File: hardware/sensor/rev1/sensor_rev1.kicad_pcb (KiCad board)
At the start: 2 copper layers, 28.9 x 68.9 mm, 52 parts, among them IC1 STM8L051F3P6, IC2 CC1101RGPR, J1 22-28-4044, J2 M20-9770342, Y1 NX3225GA-26.000M-STD-CRG-2

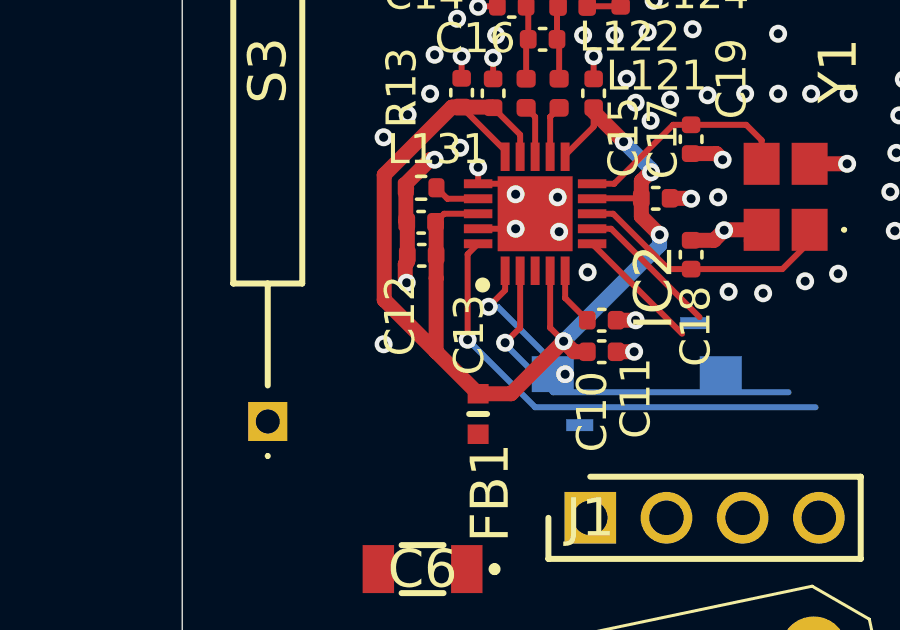
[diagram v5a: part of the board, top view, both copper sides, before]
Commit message: EG-49 Removed a bulk capacitor.
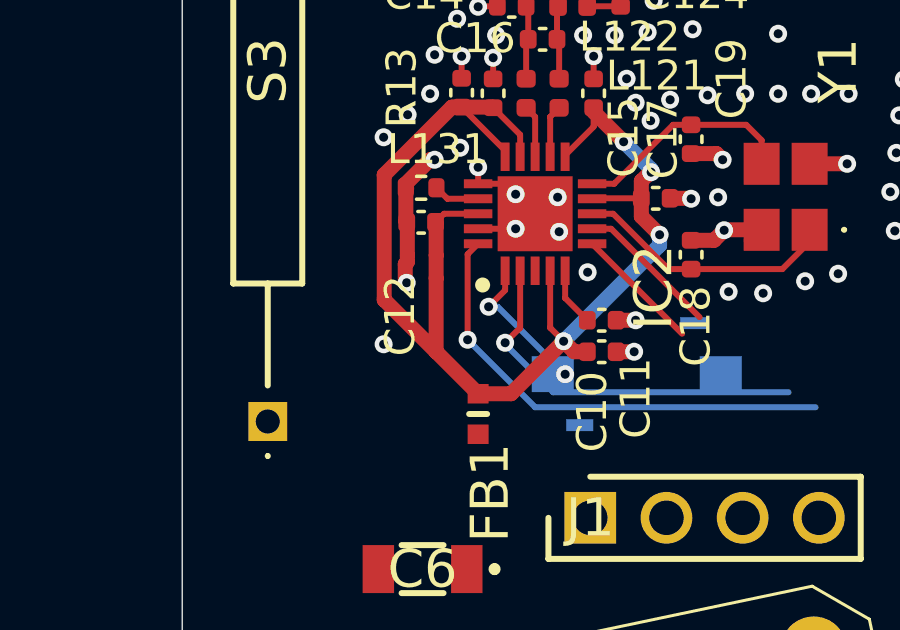
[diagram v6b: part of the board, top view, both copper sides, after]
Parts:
- removed C13: 1uF, Capacitor_SMD:C_0402_1005Metric
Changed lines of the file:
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@@
 	(net 34 "unconnected-(S2-GND_1-Pad3)")
 	(net 35 "unconnected-(S2-GND_2-Pad4)")
-	(footprint "Capacitor_SMD:C_0402_1005Metric"
-		(layer "F.Cu")
-		(at 227.9821 115.43 180)
-		(descr "Capacitor SMD 0402 (1005 Metric), square (rectangular) end terminal, IPC_7351 nominal, (Body size source: IPC-SM-782 page 76, https://www.pcb-3d.com/wordpress/wp-content/uploads/ipc-sm-782a_amendment_1_and_2.pdf), generated with kicad-footprint-generator")
-		(tags "capacitor")
-		(property "Reference" "C13"
-			(at -1.58 -2.65 90)
-			(layer "F.SilkS")
-			(effects
-				(font
-					(size 1 1)
-					(thickness 0.15)
-				)
-			)
-		)
-		(property "Value" "1uF"
-			(at 0 1.16 0)
-			(layer "F.Fab")
-			(effects
-				(font
-					(size 1 1)
-					(thickness 0.15)
-				)
-			)
-		)
-		(property "Datasheet" "~"
-			(at 0 0 180)
-			(unlocked yes)
-			(layer "F.Fab")
-			(hide yes)
-			(effects
-				(font
-					(size 1.27 1.27)
-					(thickness 0.15)
-				)
-			)
-		)
-		(property "Description" "Unpolarized capacitor"
-			(at 0 0 180)
-			(unlocked yes)
-			(layer "F.Fab")
-			(hide yes)
-			(effects
-				(font
-					(size 1.27 1.27)
-					(thickness 0.15)
-				)
-			)
-		)
-		(property "Mouser Part Number" "81-GXT155R60J105KE1D"
-			(at 0 0 180)
-			(unlocked yes)
-			(layer "F.Fab")
-			(hide yes)
-			(effects
-				(font
-					(size 1 1)
-					(thickness 0.15)
-				)
-			)
-		)
-		(property "Supplier Link" "https://pt.mouser.com/ProductDetail/Murata-Electronics/GXT155R60J105KE01D?qs=d0WKAl%252BL4Kb4JfV7cPss8A%3D%3D"
-			(at 0 0 180)
-			(unlocked yes)
-			(layer "F.Fab")
-			(hide yes)
-			(effects
-				(font
-					(size 1 1)
-					(thickness 0.15)
-				)
-			)
-		)
-		(property "Manufacturer" "Murata"
-			(at 0 0 180)
-			(unlocked yes)
-			(layer "F.Fab")
-			(hide yes)
-			(effects
-				(font
-					(size 1 1)
-					(thickness 0.15)
-				)
-			)
-		)
-		(property "Manufacturer Part Number" "GXT155R60J105KE01D "
-			(at 0 0 180)
-			(unlocked yes)
-			(layer "F.Fab")
-			(hide yes)
-			(effects
-				(font
-					(size 1 1)
-					(thickness 0.15)
-				)
-			)
-		)
-		(property ki_fp_filters "C_*")
-		(sheetname "/RF/")
-		(sheetfile "rf_rev1.kicad_sch")
-		(attr smd)
-		(fp_line
-			(start -0.107836 0.36)
-			(end 0.107836 0.36)
-			(stroke
-				(width 0.12)
-				(type solid)
-			)
-			(layer "F.SilkS")
-		)
-		(fp_line
-			(start -0.107836 -0.36)
-			(end 0.107836 -0.36)
-			(stroke
-				(width 0.12)
-				(type solid)
-			)
-			(layer "F.SilkS")
-		)
-		(fp_line
-			(start 0.91 0.46)
-			(end -0.91 0.46)
-			(stroke
-				(width 0.05)
-				(type solid)
-			)
-			(layer "F.CrtYd")
-		)
-		(fp_line
-			(start 0.91 -0.46)
-			(end 0.91 0.46)
-			(stroke
-				(width 0.05)
-				(type solid)
-			)
-			(layer "F.CrtYd")
-		)
-		(fp_line
-			(start -0.91 0.46)
-			(end -0.91 -0.46)
-			(stroke
-				(width 0.05)
-				(type solid)
-			)
-			(layer "F.CrtYd")
-		)
-		(fp_line
-			(start -0.91 -0.46)
-			(end 0.91 -0.46)
-			(stroke
-				(width 0.05)
-				(type solid)
-			)
-			(layer "F.CrtYd")
-		)
-		(fp_line
-			(start 0.5 0.25)
-			(end -0.5 0.25)
-			(stroke
-				(width 0.1)
-				(type solid)
-			)
-			(layer "F.Fab")
-		)
-		(fp_line
-			(start 0.5 -0.25)
-			(end 0.5 0.25)
-			(stroke
-				(width 0.1)
-				(type solid)
-			)
-			(layer "F.Fab")
-		)
-		(fp_line
-			(start -0.5 0.25)
-			(end -0.5 -0.25)
-			(stroke
-				(width 0.1)
-				(type solid)
-			)
-			(layer "F.Fab")
-		)
-		(fp_line
-			(start -0.5 -0.25)
-			(end 0.5 -0.25)
-			(stroke
-				(width 0.1)
-				(type solid)
-			)
-			(layer "F.Fab")
-		)
-		(fp_text user "${REFERENCE}"
-			(at 0 0 0)
-			(layer "F.Fab")
-			(effects
-				(font
-					(size 0.25 0.25)
-					(thickness 0.04)
-				)
-			)
-		)
-		(pad "1" smd roundrect
-			(at -0.48 0 180)
-			(size 0.56 0.62)
-			(layers "F.Cu" "F.Mask" "F.Paste")
-			(roundrect_rratio 0.25)
-			(net 7 "RF_VDD")
-			(pintype "passive")
-		)
-		(pad "2" smd roundrect
-			(at 0.48 0 180)
-			(size 0.56 0.62)
-			(layers "F.Cu" "F.Mask" "F.Paste")
-			(roundrect_rratio 0.25)
-			(net 1 "GND")
-			(pintype "passive")
-		)
-		(embedded_fonts no)
-		(model "${KICAD9_3DMODEL_DIR}/Capacitor_SMD.3dshapes/C_0402_1005Metric.wrl"
-			(offset
-				(xyz 0 0 0)
-			)
-			(scale
-				(xyz 1 1 1)
-			)
-			(rotate
-				(xyz 0 0 0)
-			)
-		)
-	)
 	(footprint "Resistor_SMD:R_0402_1005Metric"
 		(layer "F.Cu")

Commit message: EG-49 MCU schematic part is concluded.
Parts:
- LED1: value APTD1608LSURCK -> VLMS3000-GS08; footprint MyParts:LEDM168X95N -> MyParts:VLMS3000GS08
- R10: value 50 -> 100
- moved LED1 4.89 mm to (245.3, 80.6), turned to 0 degrees
